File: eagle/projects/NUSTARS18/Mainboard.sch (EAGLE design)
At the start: 8 parts

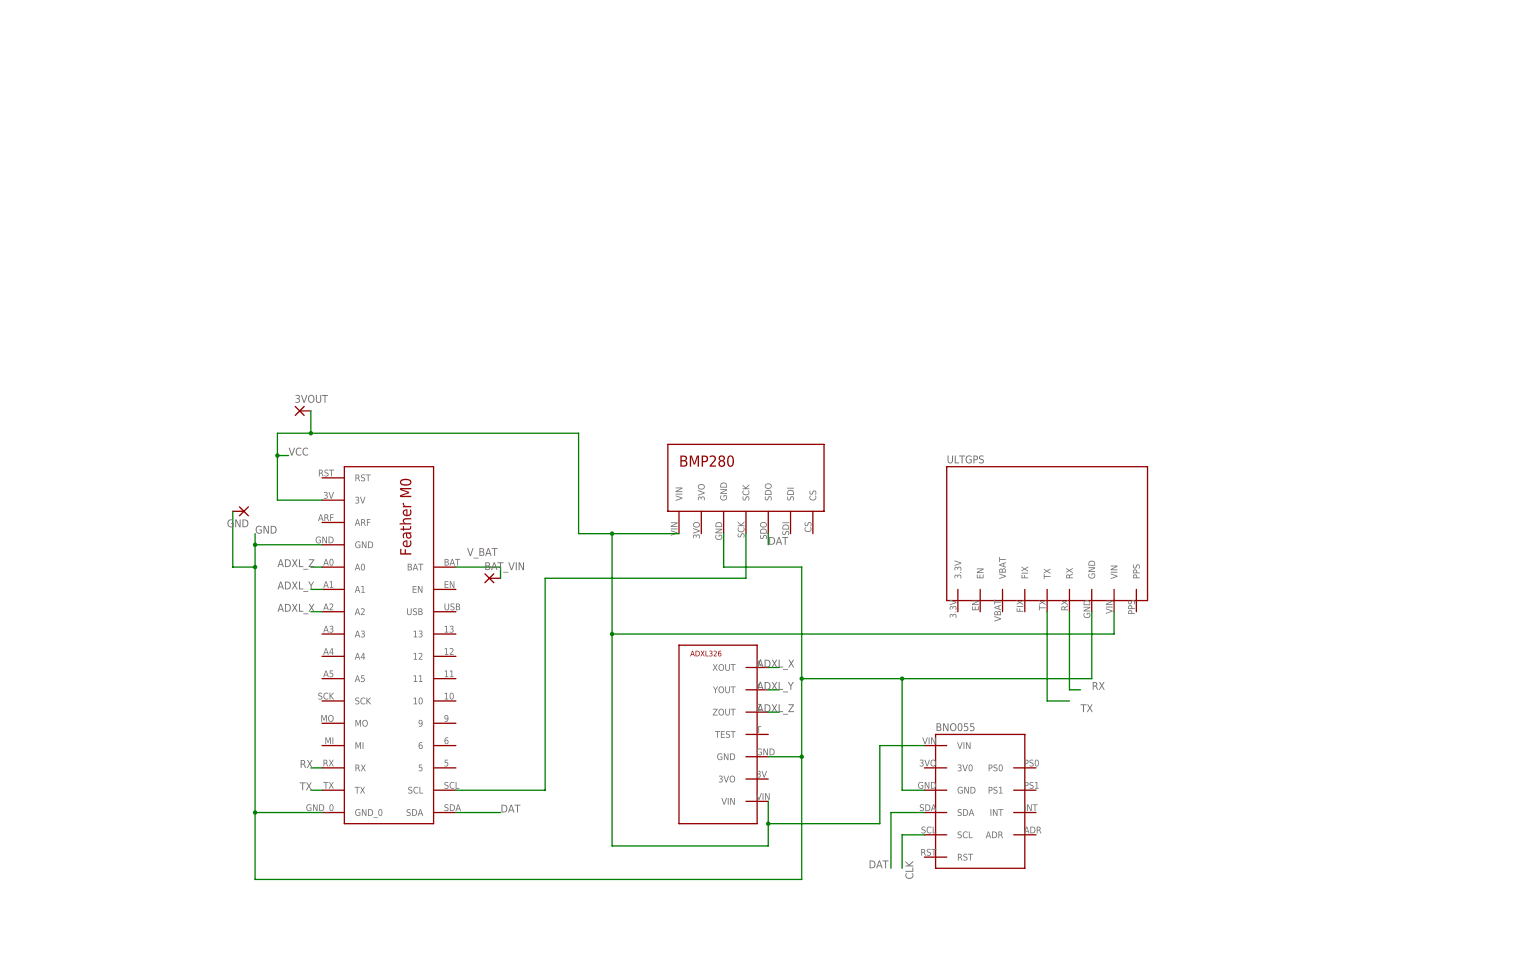
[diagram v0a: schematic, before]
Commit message: Updated board to latest requirements
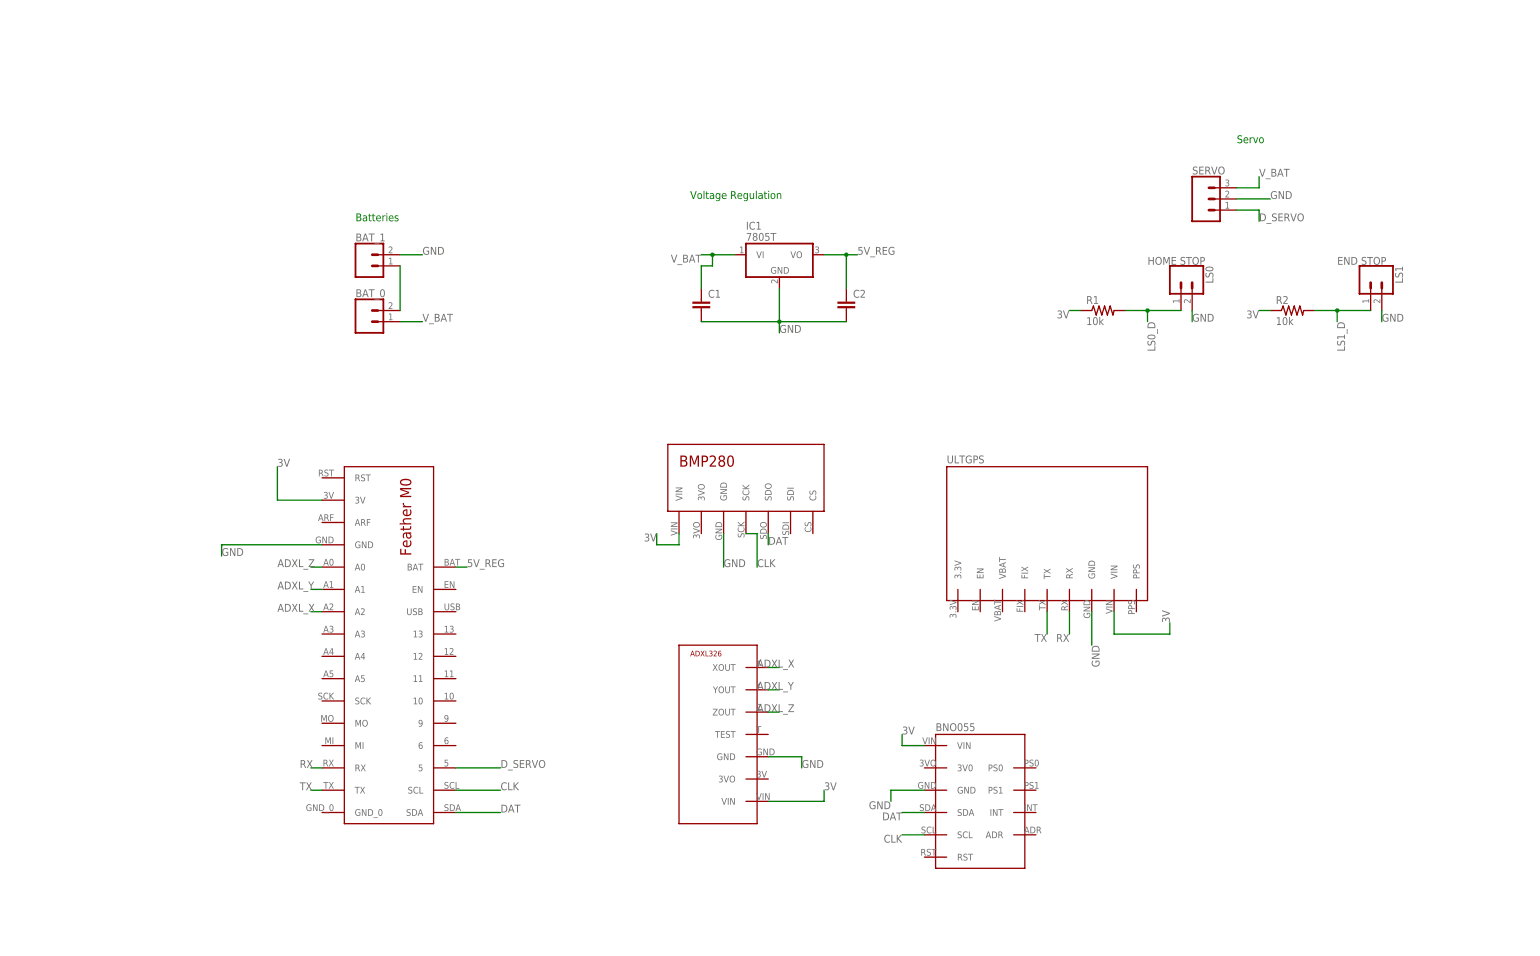
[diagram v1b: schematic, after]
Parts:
- removed 3VOUT, BAT_VIN, GND: (no value), wirepad:2,15/1,0
- added BAT_0, BAT_1: (no value), SparkFun-Connectors:CONN_02JST-PTH-2
- added C1, C2: (no value), capacitor-wima:C2,5-3
- added IC1: 7805T, linear:7805T
- added LS0: HOME STOP, SparkFun-Connectors:CONN_02JST-PTH-2
- added LS1: END STOP, SparkFun-Connectors:CONN_02JST-PTH-2
- added R1, R2: 10k, rcl:R-US_0207/10
- added SERVO: (no value), SparkFun-Connectors:CONN_03JST-PTH
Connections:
- removed net VCC: 3VOUT.P, U$1.3V, U$2.VIN, U$3.VIN, U$4.VIN, U$5.VIN
- new net 3V: R1.1, R2.1, U$1.3V, U$2.VIN, U$3.VIN, U$4.VIN, U$5.VIN
- new net 5V_REG: C2.1, IC1.VO, U$1.BAT
- new net B_INT: BAT_0.2, BAT_1.1
- new net D_SERVO: SERVO.1, U$1.5
- new net LS0_D: LS0.1, R1.2
- new net LS1_D: LS1.1, R2.2
- net GND: now also BAT_1.2, C1.2, C2.2, IC1.GND, LS0.2, LS1.2, SERVO.2; no longer GND.P, U$1.GND_0
- net V_BAT: now also BAT_0.1, C1.1, IC1.VI, SERVO.3; no longer BAT_VIN.P, U$1.BAT
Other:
- note added: "Batteries"
- note added: "Servo"
- note added: "Voltage Regulation"

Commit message: Updated the board yet again
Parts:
- removed IC1: 7805T, linear:7805T
- added IC0: 7805T, linear:7805T
- C1, C2: value (none) -> 10uF
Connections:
- removed net 5V_REG: C2.1, IC1.VO, U$1.BAT
- new net 5V_REG_M0: C2.1, IC0.VO, U$1.BAT
- net ADXL_X: now also U$1.A3; no longer U$1.A2
- net ADXL_Y: now also U$1.A2; no longer U$1.A1
- net ADXL_Z: now also U$1.A1; no longer U$1.A0
- net GND: now also IC0.GND; no longer IC1.GND
- net LS0_D: now also U$1.10
- net LS1_D: now also U$1.6
- net V_BAT: now also IC0.VI; no longer IC1.VI
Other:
- moved on the sheet: BAT_0, BAT_1, C1, C2, LS0, LS1, R1, R2, SERVO

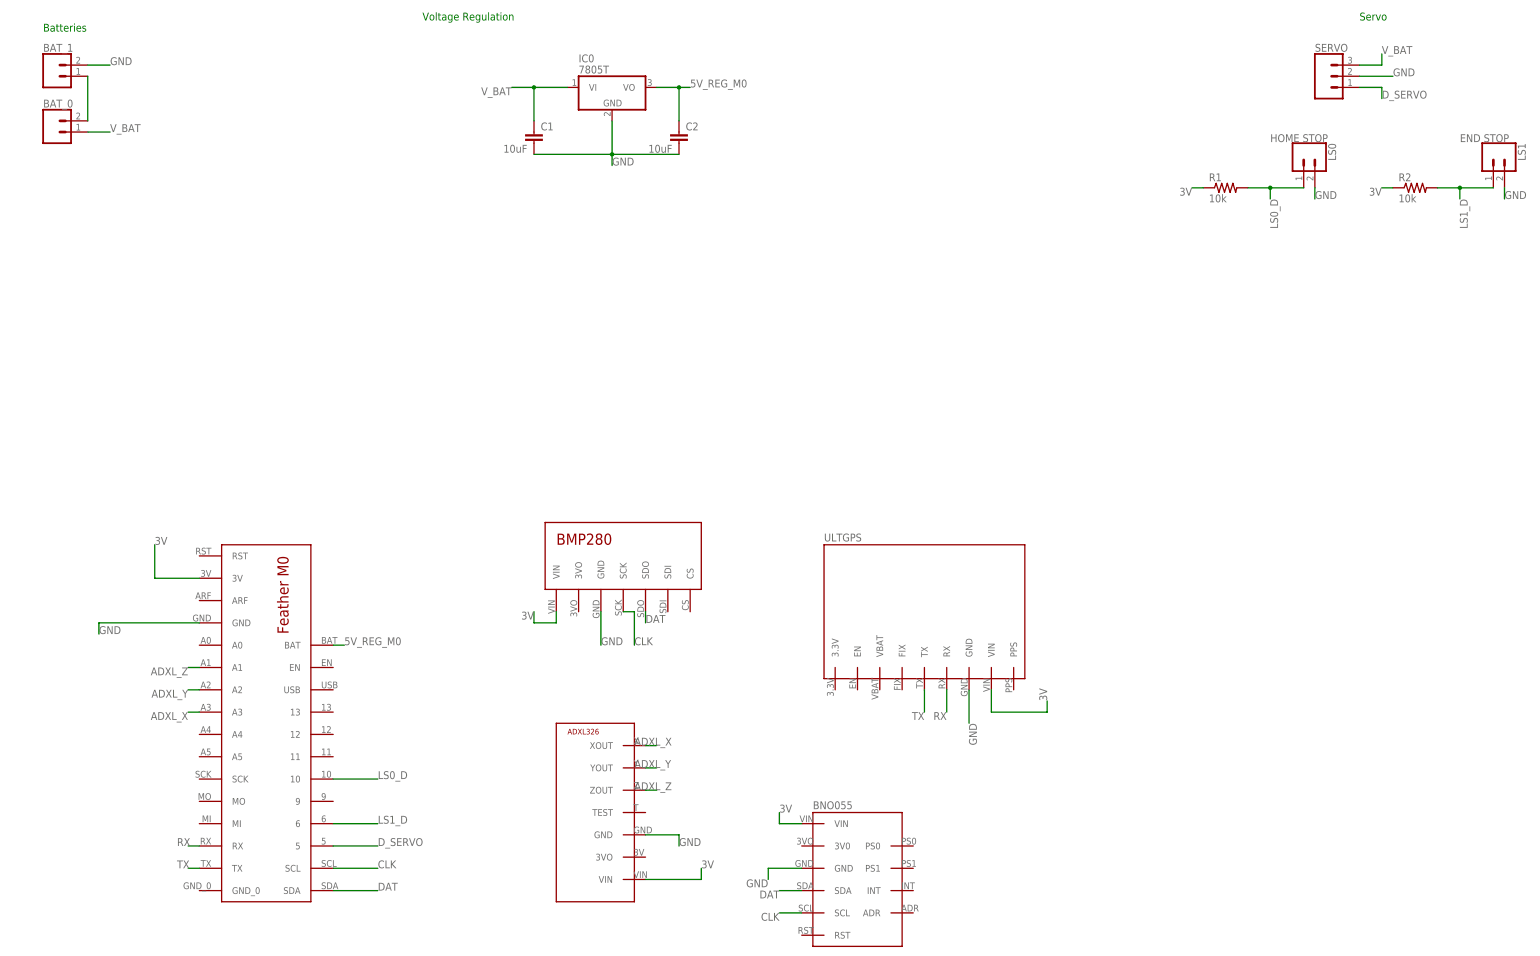
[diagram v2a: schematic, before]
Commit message: Added Raven JST to board
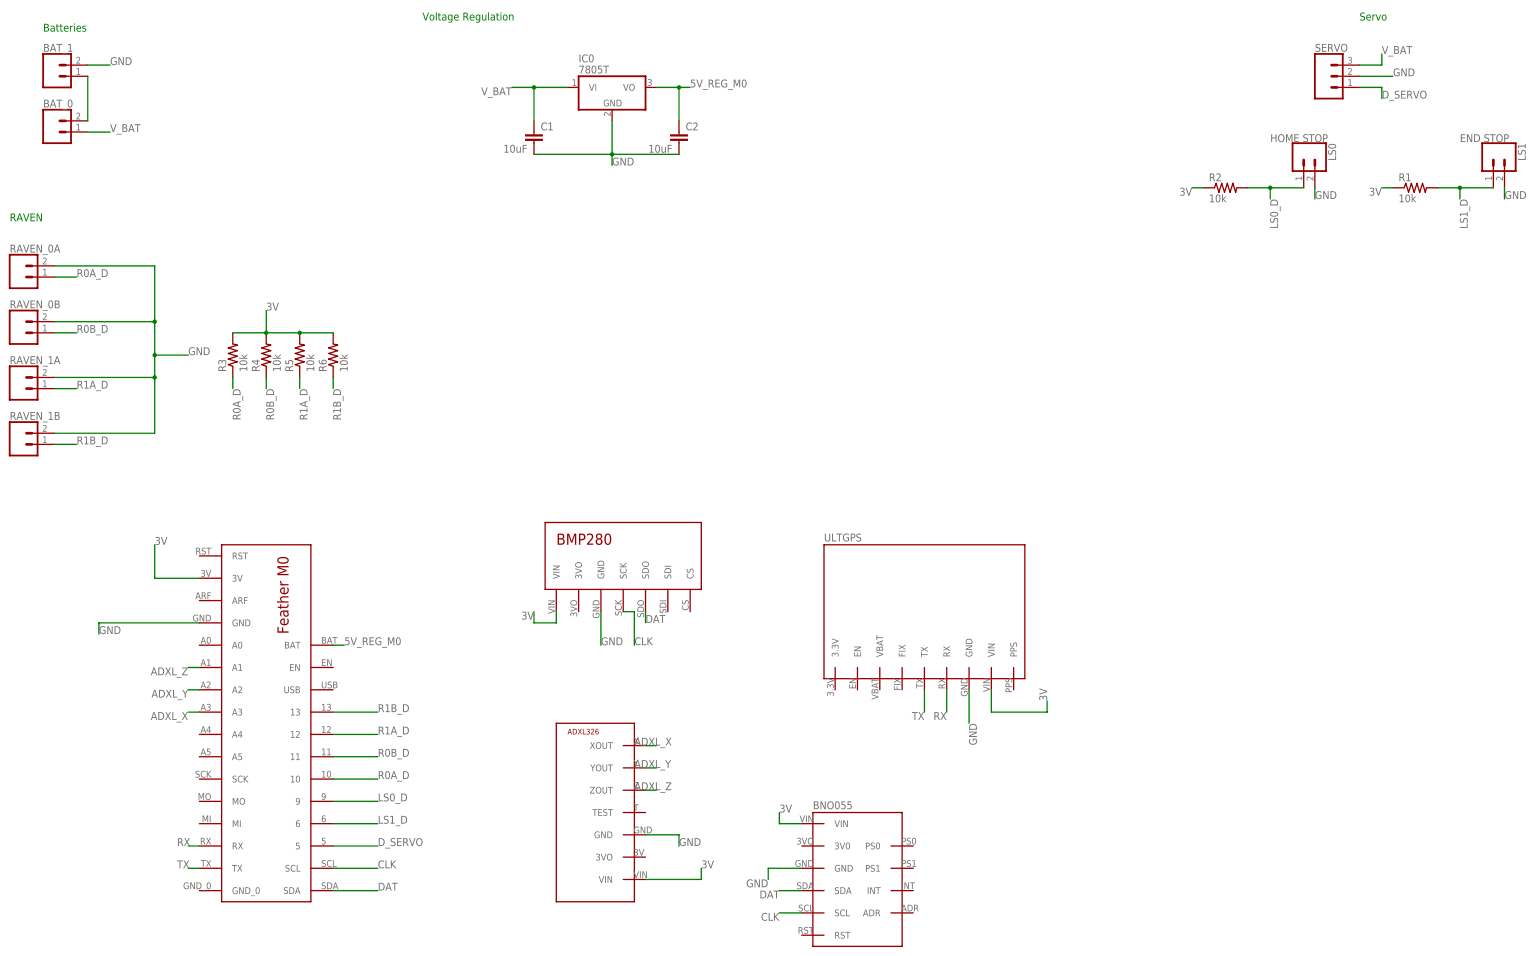
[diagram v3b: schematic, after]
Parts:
- added R3, R4, R5, R6: 10k, rcl:R-US_0207/10
- added RAVEN_0A, RAVEN_0B, RAVEN_1A, RAVEN_1B: (no value), SparkFun-Connectors:CONN_02JST-PTH-2
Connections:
- new net R0A_D: R3.1, RAVEN_0A.1, U$1.10
- new net R0B_D: R4.1, RAVEN_0B.1, U$1.11
- new net R1A_D: R5.1, RAVEN_1A.1, U$1.12
- new net R1B_D: R6.1, RAVEN_1B.1, U$1.13
- net 3V: now also R3.2, R4.2, R5.2, R6.2
- net GND: now also RAVEN_0A.2, RAVEN_0B.2, RAVEN_1A.2, RAVEN_1B.2
- net LS0_D: now also R2.2, U$1.9; no longer R1.2, U$1.10
- net LS1_D: now also R1.2; no longer R2.2
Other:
- note added: "RAVEN"
- moved on the sheet: R1, R2

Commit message: Added mass analysis and general board improvements
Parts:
- added BAT_7.4V, BAT_GND: (no value), wirepad:3,81/1,4
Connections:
- net GND: now also BAT_GND.P
- net V_BAT: now also BAT_7.4V.P
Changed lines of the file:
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@@
 <part name="R5" library="rcl" library_urn="urn:adsk.eagle:library:334" deviceset="R-US_" device="0207/10" package3d_urn="urn:adsk.eagle:package:23491/1" value="10k"/>
 <part name="R6" library="rcl" library_urn="urn:adsk.eagle:library:334" deviceset="R-US_" device="0207/10" package3d_urn="urn:adsk.eagle:package:23491/1" value="10k"/>
+<part name="BAT_7.4V" library="wirepad" library_urn="urn:adsk.eagle:library:412" deviceset="3,81/1,4" device="" package3d_urn="urn:adsk.eagle:package:30835/1"/>
+<part name="BAT_GND" library="wirepad" library_urn="urn:adsk.eagle:library:412" deviceset="3,81/1,4" device="" package3d_urn="urn:adsk.eagle:package:30835/1"/>
 </parts>
 <sheets>
@@
 <attribute name="VALUE" x="-9.398" y="110.49" size="1.778" layer="96" rot="R90"/>
 </instance>
+<instance part="BAT_7.4V" gate="1" x="-38.1" y="165.1" smashed="yes" rot="R180">
+<attribute name="NAME" x="-36.957" y="163.2458" size="1.778" layer="95" rot="R180"/>
+<attribute name="VALUE" x="-36.957" y="168.402" size="1.778" layer="96" rot="R180"/>
+</instance>
+<instance part="BAT_GND" gate="1" x="-38.1" y="180.34" smashed="yes" rot="R180">
+<attribute name="NAME" x="-36.957" y="178.4858" size="1.778" layer="95" rot="R180"/>
+<attribute name="VALUE" x="-36.957" y="183.642" size="1.778" layer="96" rot="R180"/>
+</instance>
 </instances>
 <busses>
@@
 </segment>
 <segment>
-<wire x1="-68.58" y1="180.34" x2="-63.5" y2="180.34" width="0.1524" layer="91"/>
 <label x="-63.5" y="180.34" size="1.778" layer="95"/>
 <pinref part="BAT_1" gate="G$1" pin="2"/>
+<pinref part="BAT_GND" gate="1" pin="P"/>
+<wire x1="-68.58" y1="180.34" x2="-40.64" y2="180.34" width="0.1524" layer="91"/>
 </segment>
 <segment>
@@
 <net name="V_BAT" class="0">
 <segment>
-<wire x1="-68.58" y1="165.1" x2="-63.5" y2="165.1" width="0.1524" layer="91"/>
 <label x="-63.5" y="165.1" size="1.778" layer="95"/>
 <pinref part="BAT_0" gate="G$1" pin="1"/>
-</segment>
-<segment>
+<pinref part="BAT_7.4V" gate="1" pin="P"/>
+<wire x1="-40.64" y1="165.1" x2="-68.58" y2="165.1" width="0.1524" layer="91"/>
+</segment>
+<segment>
